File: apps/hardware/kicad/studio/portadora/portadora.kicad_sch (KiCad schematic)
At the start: 64 parts, among them J1 Teensy 4.1 izq, J10 5V desde USB-C de panel, J11 OUT L 1/4 NRJ3HF-1, J12 OUT R 1/4 NRJ3HF-1, J13 PHONES 3.5 sleeve HP_VGND, J14 CV OUT 3.5, J15 Shield fila 13-5V, J16 Shield fila 12-GND, J2 Teensy 4.1 der, J3 USB host Teensy, J5 Panel IDC 2x15, J6 Raspberry Pi pines 1-10, J7 IN L 1/4 NRJ3HF-1, J8 IN R 1/4 NRJ3HF-1, J9 Audio Shield LINE y HP, SW1 PAD 0 -10 -20 dB, U1 74AHCT1G125, U2 MCP6004

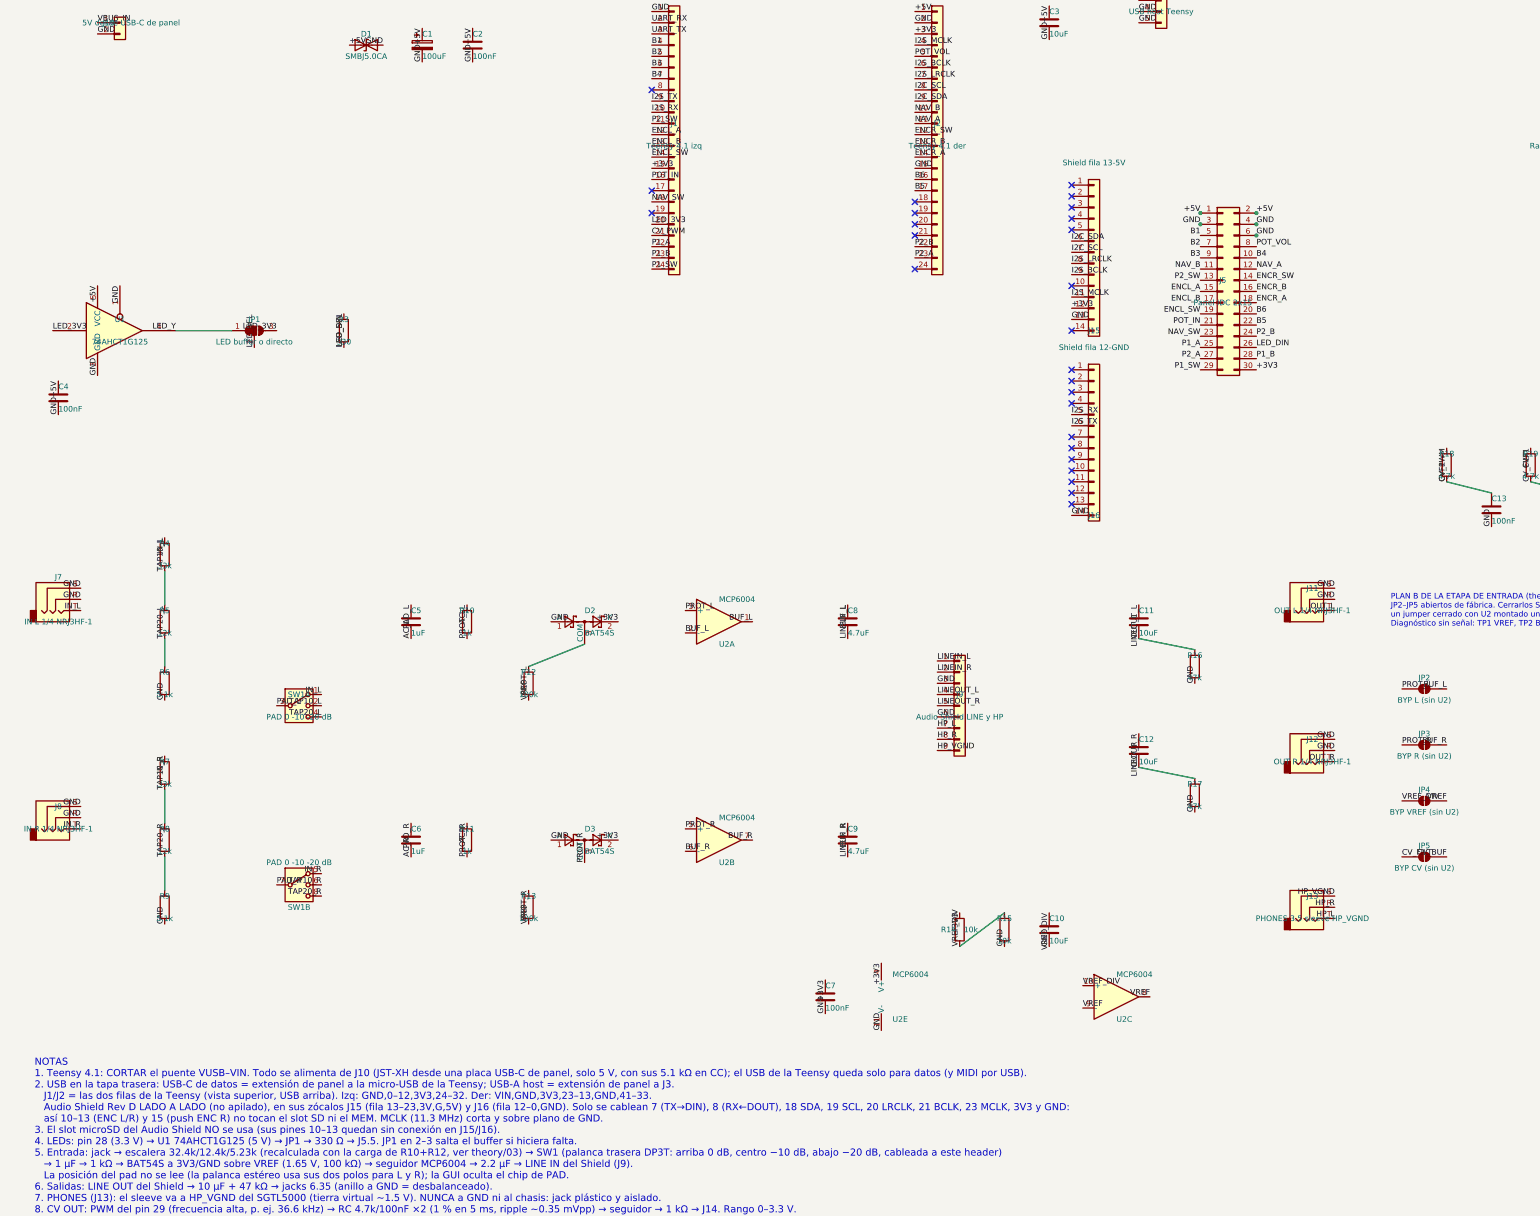
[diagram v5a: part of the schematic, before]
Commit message: fix(studio): ENC R-A pasa del pin 13 al pin 6 (auditoría de fabricación F1)
El pin 13 de la Teensy 4.1 tiene el LED con 470 Ω a GND: con el INPUT_PULLUP de Encoder la
fase A puede no llegar a HIGH. Aprobado por Juan: pin 6, el único que 01 §3.3 no reserva
(en Studio es el MEMCS del shield, que no se cablea). 01 §3.3 enmendado; portadora:
etiqueta ENCR_A en J1.8 y solo esa red re-ruteada (J5.18 → J1.8), DRC 0 / paridad 0 /
ERC 0 errores; gerbers regenerados (BOM y CPL sin cambios). Firmware: enc_r(6, 14).

Co-Authored-By: Claude Opus 5.5 <noreply@anthropic.com>
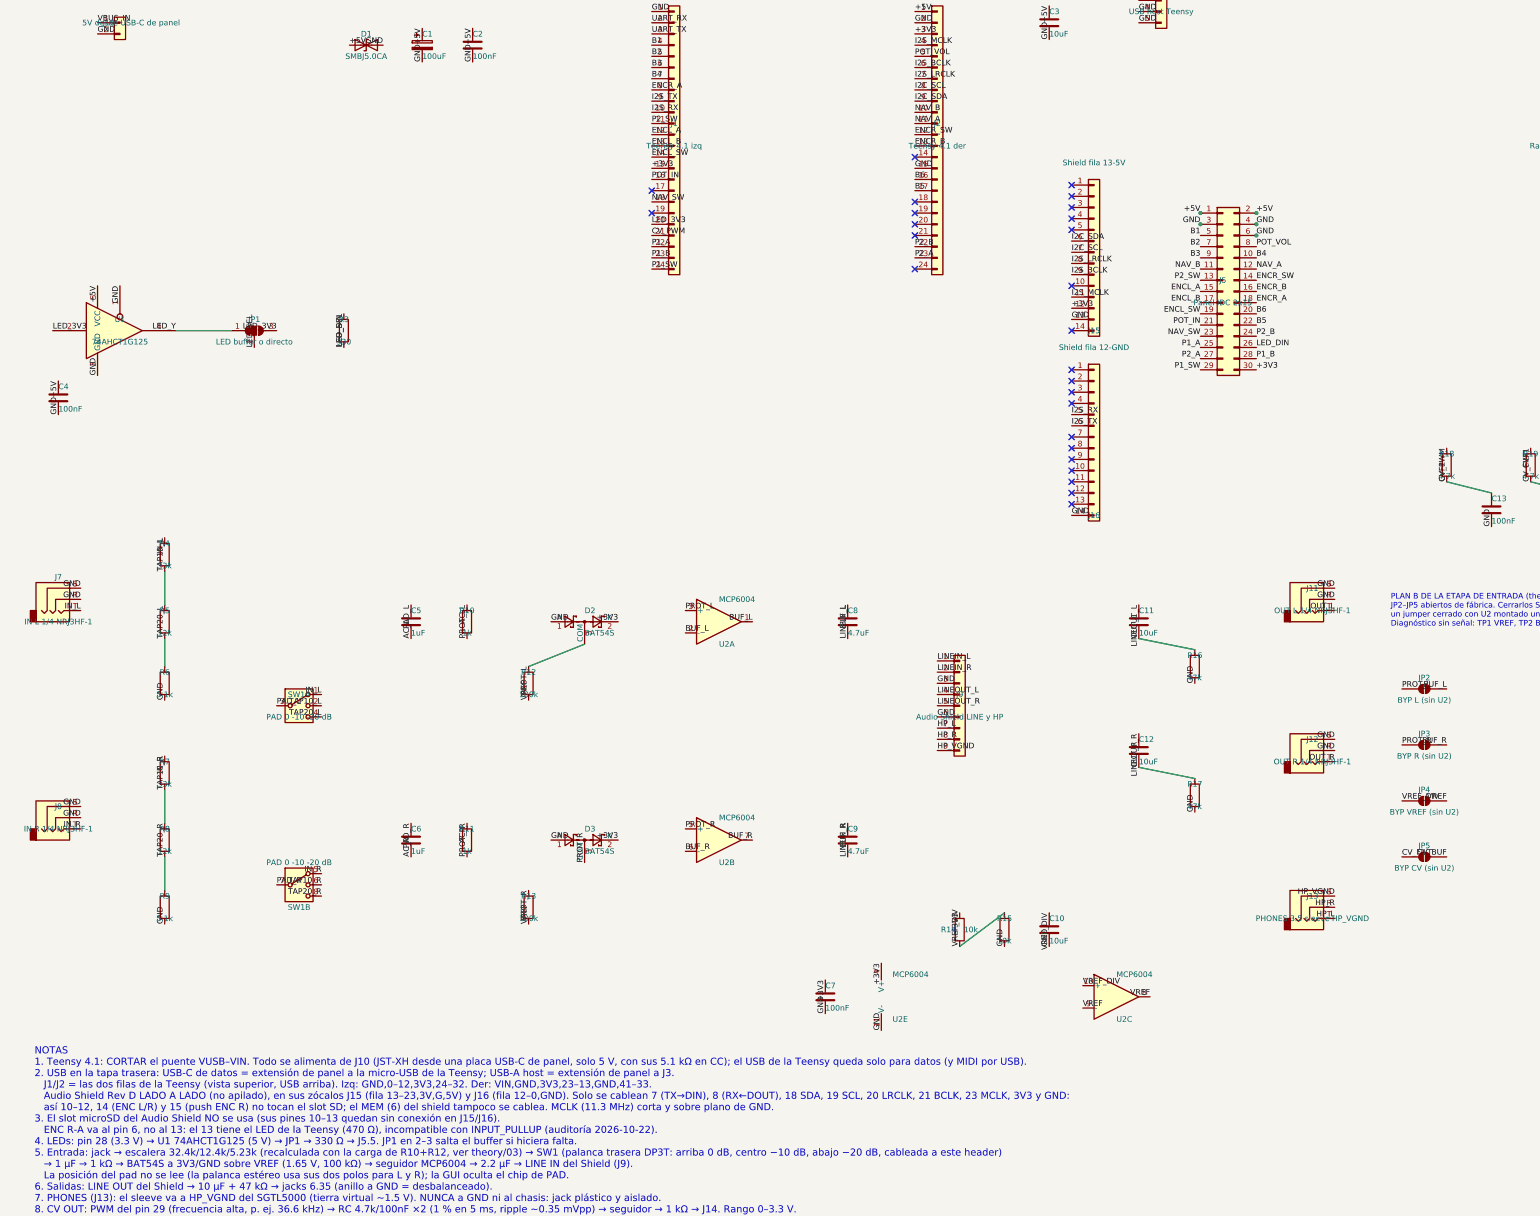
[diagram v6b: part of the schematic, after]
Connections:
- net ENCR_A: now also J1.8 (Pin_8); no longer J2.14 (Pin_14)
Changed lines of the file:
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@@
 	)
 	(label "ENCR_A"
-		(at 219.70999999999998 80.01 0)
+		(at 160.02 64.77 0)
 		(effects
 			(font
@@
 	)
 	(no_connect
-		(at 160.01999999999998 64.77000000000001)
+		(at 219.71 80.01)
 	)
 	(no_connect
@@
 		)
 	)
-	(text "NOTAS\n1. Teensy 4.1: CORTAR el puente VUSB–VIN. Todo se alimenta de J10 (JST-XH desde una placa USB-C de panel, solo 5 V, con sus 5.1 kΩ en CC); el USB de la Teensy queda solo para datos (y MIDI por USB).\n2. USB en la tapa trasera: USB-C de datos = extensión de panel a la micro-USB de la Teensy; USB-A host = extensión de panel a J3.\n   J1/J2 = las dos filas de la Teensy (vista superior, USB arriba). Izq: GND,0–12,3V3,24–32. Der: VIN,GND,3V3,23–13,GND,41–33.\n   Audio Shield Rev D LADO A LADO (no apilado), en sus zócalos J15 (fila 13–23,3V,G,5V) y J16 (fila 12–0,GND). Solo se cablean 7 (TX→DIN), 8 (RX←DOUT), 18 SDA, 19 SCL, 20 LRCLK, 21 BCLK, 23 MCLK, 3V3 y GND:\n   así 10–13 (ENC L/R) y 15 (push ENC R) no tocan el slot SD ni el MEM. MCLK (11.3 MHz) corta y sobre plano de GND.\n3. El slot microSD del Audio Shield NO se usa (sus pines 10–13 quedan sin conexión en J15/J16).\n4. LEDs: pin 28 (3.3 V) → U1 74AHCT1G125 (5 V) → JP1 → 330 Ω → J5.5. JP1 en 2–3 salta el buffer si hiciera falta.\n5. Entrada: jack → escalera 32.4k/12.4k/5.23k (recalculada con la carga de R10+R12, ver theory/03) → SW1 (palanca trasera DP3T: arriba 0 dB, centro −10 dB, abajo −20 dB, cableada a este header)\n   → 1 µF → 1 kΩ → BAT54S a 3V3/GND sobre VREF (1.65 V, 100 kΩ) → seguidor MCP6004 → 2.2 µF → LINE IN del Shield (J9).\n   La posición del pad no se lee (la palanca estéreo usa sus dos polos para L y R); la GUI oculta el chip de PAD.\n6. Salidas: LINE OUT del Shield → 10 µF + 47 kΩ → jacks 6.35 (anillo a GND = desbalanceado).\n7. PHONES (J13): el sleeve va a HP_VGND del SGTL5000 (tierra virtual ~1.5 V). NUNCA a GND ni al chasis: jack plástico y aislado.\n8. CV OUT: PWM del pin 29 (frecuencia alta, p. ej. 36.6 kHz) → RC 4.7k/100nF ×2 (1 % en 5 ms, ripple ~0.35 mVpp) → seguidor → 1 kΩ → J14. Rango 0–3.3 V.\n9. Pi (J6, header de la Pi pines 1–10): 5 V en 2 y 4, GND en 6 y 9, Teensy RX0 ← Pi TXD (GPIO14, pin 8), Teensy TX1 → Pi RXD (GPIO15, pin 10).\n   Hacer el cable con dos hilos por 5 V y por GND."
+	(text "NOTAS\n1. Teensy 4.1: CORTAR el puente VUSB–VIN. Todo se alimenta de J10 (JST-XH desde una placa USB-C de panel, solo 5 V, con sus 5.1 kΩ en CC); el USB de la Teensy queda solo para datos (y MIDI por USB).\n2. USB en la tapa trasera: USB-C de datos = extensión de panel a la micro-USB de la Teensy; USB-A host = extensión de panel a J3.\n   J1/J2 = las dos filas de la Teensy (vista superior, USB arriba). Izq: GND,0–12,3V3,24–32. Der: VIN,GND,3V3,23–13,GND,41–33.\n   Audio Shield Rev D LADO A LADO (no apilado), en sus zócalos J15 (fila 13–23,3V,G,5V) y J16 (fila 12–0,GND). Solo se cablean 7 (TX→DIN), 8 (RX←DOUT), 18 SDA, 19 SCL, 20 LRCLK, 21 BCLK, 23 MCLK, 3V3 y GND:\n   así 10–12, 14 (ENC L/R) y 15 (push ENC R) no tocan el slot SD; el MEM (6) del shield tampoco se cablea. MCLK (11.3 MHz) corta y sobre plano de GND.\n3. El slot microSD del Audio Shield NO se usa (sus pines 10–13 quedan sin conexión en J15/J16).\n   ENC R-A va al pin 6, no al 13: el 13 tiene el LED de la Teensy (470 Ω), incompatible con INPUT_PULLUP (auditoría 2026-10-22).\n4. LEDs: pin 28 (3.3 V) → U1 74AHCT1G125 (5 V) → JP1 → 330 Ω → J5.5. JP1 en 2–3 salta el buffer si hiciera falta.\n5. Entrada: jack → escalera 32.4k/12.4k/5.23k (recalculada con la carga de R10+R12, ver theory/03) → SW1 (palanca trasera DP3T: arriba 0 dB, centro −10 dB, abajo −20 dB, cableada a este header)\n   → 1 µF → 1 kΩ → BAT54S a 3V3/GND sobre VREF (1.65 V, 100 kΩ) → seguidor MCP6004 → 2.2 µF → LINE IN del Shield (J9).\n   La posición del pad no se lee (la palanca estéreo usa sus dos polos para L y R); la GUI oculta el chip de PAD.\n6. Salidas: LINE OUT del Shield → 10 µF + 47 kΩ → jacks 6.35 (anillo a GND = desbalanceado).\n7. PHONES (J13): el sleeve va a HP_VGND del SGTL5000 (tierra virtual ~1.5 V). NUNCA a GND ni al chasis: jack plástico y aislado.\n8. CV OUT: PWM del pin 29 (frecuencia alta, p. ej. 36.6 kHz) → RC 4.7k/100nF ×2 (1 % en 5 ms, ripple ~0.35 mVpp) → seguidor → 1 kΩ → J14. Rango 0–3.3 V.\n9. Pi (J6, header de la Pi pines 1–10): 5 V en 2 y 4, GND en 6 y 9, Teensy RX0 ← Pi TXD (GPIO14, pin 8), Teensy TX1 → Pi RXD (GPIO15, pin 10).\n   Hacer el cable con dos hilos por 5 V y por GND."
 		(exclude_from_sim no)
 		(at 20 325 0)
